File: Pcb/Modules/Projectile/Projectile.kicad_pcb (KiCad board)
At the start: 2 copper layers, 108.7 x 45.7 mm, 39 parts, among them J1 JACK_RJ45, Q1 Q_NMOS_GSD, Q2 Q_NMOS_GSD, U1 OPA320, U2 OPA320, X1 HOLE, X2 HOLE, X3 HOLE, X4 HOLE

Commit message: Add some missing text to silkscreen.  Move mount holes by 5 mils.
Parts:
- moved X1 0.13 mm to (112.5, 66.0)
- moved X4 0.13 mm to (112.5, 27.9)
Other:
- board text added: "Light1"
- board text added: "Light2"
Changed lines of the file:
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@@
     (area 25.683869 23.4618 137.997001 70.6182)
     (thickness 1.6)
-    (drawings 5)
+    (drawings 15)
     (tracks 220)
     (zones 0)
@@
     (zone_45_only yes)
     (trace_min 0.2)
-    (segment_width 0.2)
+    (segment_width 2.54)
     (edge_width 0.15)
     (via_size 0.6604)
@@
   )
   (module Mounting_Holes:MountingHole_2.5mm_Pad (layer F.Cu)
-    (at 112.395 66.04)
+    (at 112.522 66.04)
     (descr "Mounting Hole 2.5mm")
     (tags "mounting hole 2.5mm")
@@
   )
   (module Mounting_Holes:MountingHole_2.5mm_Pad (layer F.Cu)
-    (at 112.395 27.94)
+    (at 112.522 27.94)
     (descr "Mounting Hole 2.5mm")
     (tags "mounting hole 2.5mm")
@@
     )
   )
+  (gr_text Light2 (at 137.668 48.387) (layer F.SilkS)
+    (effects (font (size 1.5 1.5) (thickness 0.3)) (justify right))
+  )
+  (gr_text Light1 (at 29.337 48.387) (layer F.SilkS)
+    (effects (font (size 1.5 1.5) (thickness 0.3)) (justify left))
+  )
+  (gr_line (start 105.41 57.15) (end 104.14 57.15) (angle 90) (layer F.SilkS) (width 2.54))
+  (gr_line (start 105.41 60.96) (end 105.41 57.15) (angle 90) (layer F.SilkS) (width 2.54))
+  (gr_line (start 102.87 63.5) (end 105.41 60.96) (angle 90) (layer F.SilkS) (width 2.54))
+  (gr_line (start 102.87 55.88) (end 102.87 63.5) (angle 90) (layer F.SilkS) (width 2.54))
+  (gr_line (start 101.6 67.31) (end 109.22 59.69) (angle 90) (layer F.SilkS) (width 2.54))
+  (gr_line (start 101.6 52.07) (end 101.6 67.31) (angle 90) (layer F.SilkS) (width 2.54))
+  (gr_line (start 109.22 59.69) (end 101.6 52.07) (angle 90) (layer F.SilkS) (width 2.54))
+  (gr_line (start 55.88 59.69) (end 109.22 59.69) (angle 90) (layer F.SilkS) (width 2.54))
   (gr_line (start 137.922 69.85) (end 137.922 24.13) (angle 90) (layer Edge.Cuts) (width 0.15))
   (gr_line (start 29.21 24.13) (end 29.21 69.85) (angle 90) (layer Edge.Cuts) (width 0.15))

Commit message: Update module pcbs
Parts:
- D1, D2, D3, D4, D5, D6: moved to B.Cu
- J1: moved to F.Cu
- moved D1 2.54 mm to (32.8, 61.0), turned to 90 degrees
- moved D2 2.54 mm to (32.8, 54.4), turned to 90 degrees
- moved D4 2.54 mm to (134.4, 54.4), turned to 90 degrees
- moved D6 2.54 mm to (134.4, 61.0), turned to 90 degrees
- moved D3 2.54 mm to (32.8, 67.6), turned to 90 degrees
- moved D5 2.54 mm to (134.4, 67.6), turned to 90 degrees
- turned J1 to 270 degrees
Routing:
- net 3V3: track 270.9 -> 259.6 mm
- net Net-(D4-Pad1): track 21.0 -> 29.8 mm
- net Net-(D2-Pad1): track 21.9 -> 28.2 mm
- net Net-(J1-Pad3): track 101.4 -> 104.8 mm
- net Net-(J1-Pad2): track 60.7 -> 62.1 mm, vias 0 -> 1
- net Net-(C6-Pad2): track 9.62 -> 8.58 mm
- net Net-(J1-Pad4): track 114.4 -> 113.7 mm
- net Net-(C4-Pad2): track 8.79 -> 9.41 mm
- net Net-(D2-Pad2): track 4.35 -> 4.86 mm
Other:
- board text added: "Projectile Module 2018.3.31"
- board text removed: "Projectile Module 2017.12.23"

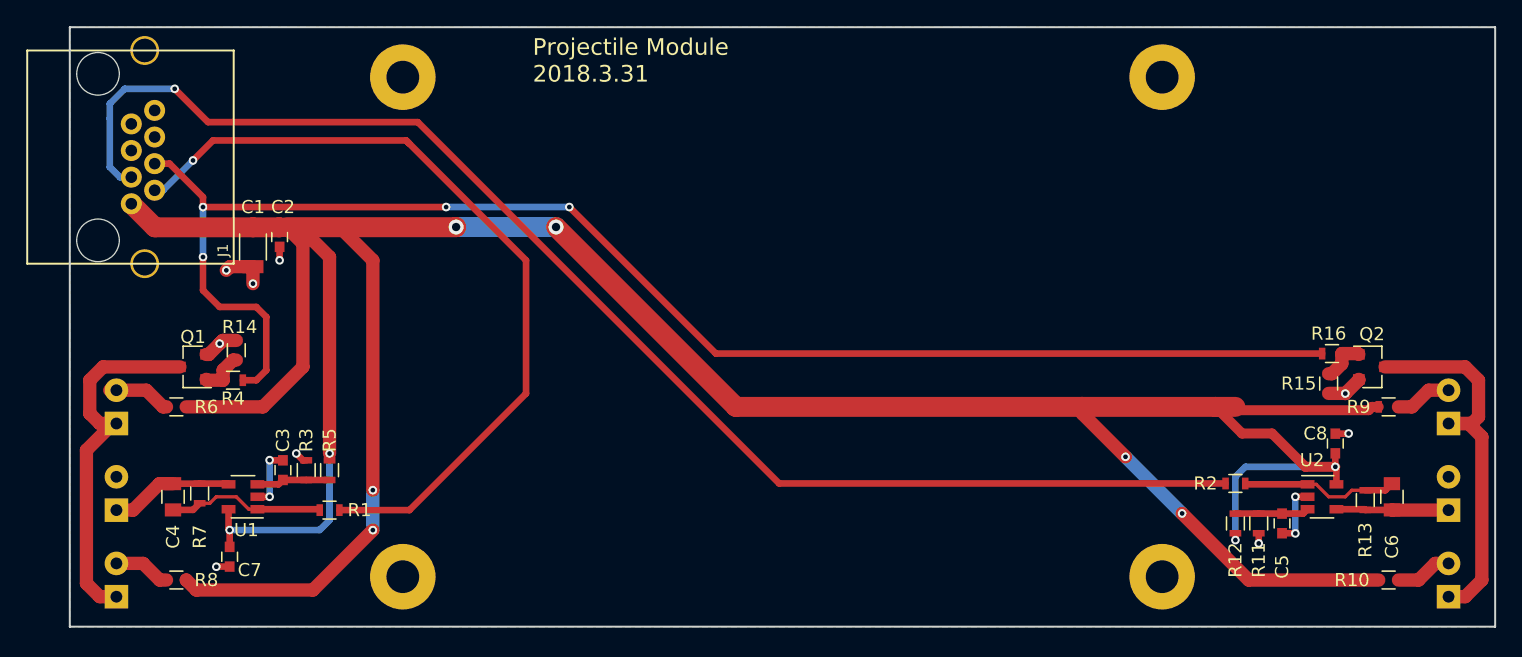
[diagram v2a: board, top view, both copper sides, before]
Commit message: Update module pcbs to fix minor issues and round corners
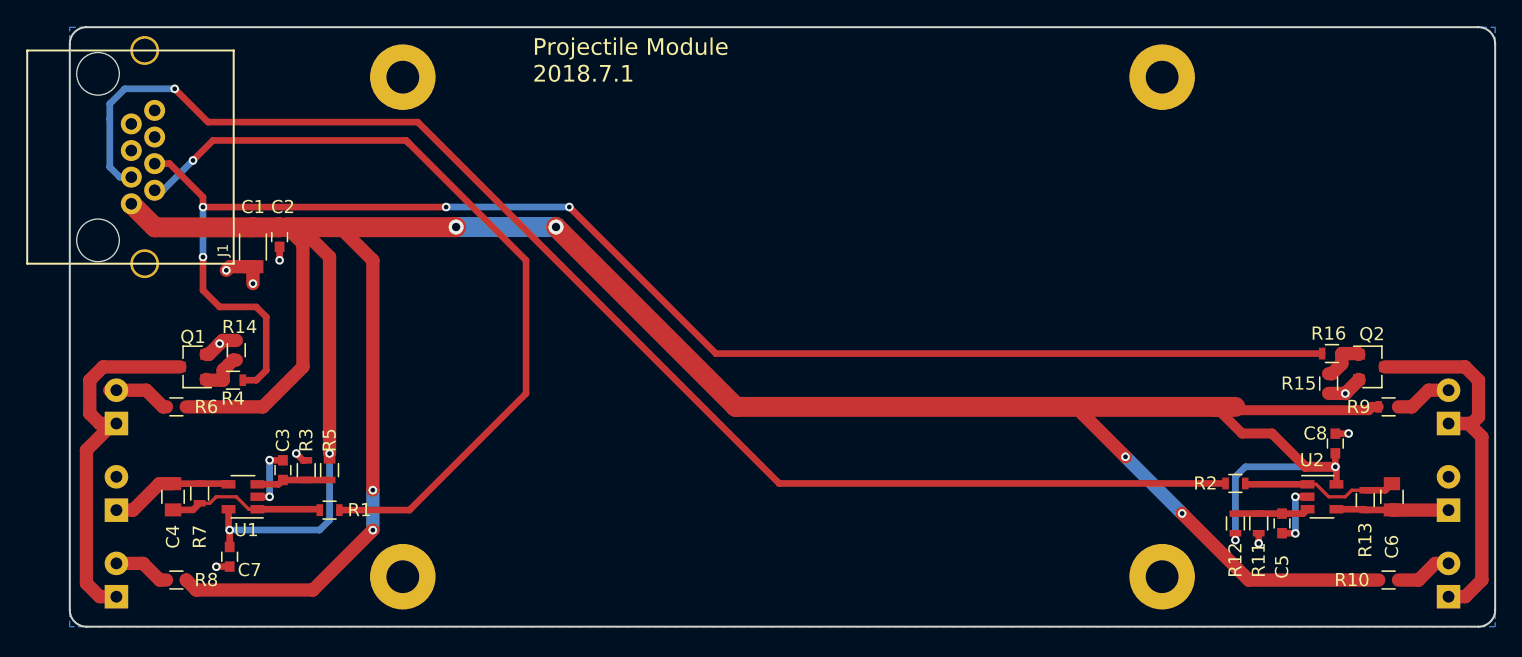
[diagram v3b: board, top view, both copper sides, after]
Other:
- outline, holes or cut-outs redrawn
- board text added: "Projectile Module 2018.7.1"
- board text removed: "Projectile Module 2018.3.31"
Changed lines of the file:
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@@
     (area 25.683869 23.4618 137.997001 70.6182)
     (thickness 1.6)
-    (drawings 15)
+    (drawings 19)
     (tracks 229)
     (zones 0)
@@
     )
   )
+  (gr_line (start 29.21 68.58) (end 29.21 25.4) (angle 90) (layer Edge.Cuts) (width 0.15))
+  (gr_line (start 136.652 69.85) (end 30.48 69.85) (angle 90) (layer Edge.Cuts) (width 0.15))
+  (gr_line (start 137.922 25.4) (end 137.922 68.58) (angle 90) (layer Edge.Cuts) (width 0.15))
+  (gr_line (start 30.48 24.13) (end 136.652 24.13) (angle 90) (layer Edge.Cuts) (width 0.15))
+  (gr_arc (start 30.48 68.58) (end 30.48 69.85) (angle 90) (layer Edge.Cuts) (width 0.15))
+  (gr_arc (start 30.48 25.4) (end 29.21 25.4) (angle 90) (layer Edge.Cuts) (width 0.15))
+  (gr_arc (start 136.652 25.4) (end 136.652 24.13) (angle 90) (layer Edge.Cuts) (width 0.15))
+  (gr_arc (start 136.652 68.58) (end 137.922 68.58) (angle 90) (layer Edge.Cuts) (width 0.15))
   (gr_line (start 55.88 59.69) (end 109.22 59.69) (angle 90) (layer B.SilkS) (width 2.54))
   (gr_text Light2 (at 130.81 48.514) (layer B.SilkS)
@@
   (gr_line (start 101.6 52.07) (end 101.6 67.31) (angle 90) (layer B.SilkS) (width 2.54))
   (gr_line (start 109.22 59.69) (end 101.6 52.07) (angle 90) (layer B.SilkS) (width 2.54))
-  (gr_line (start 137.922 69.85) (end 137.922 24.13) (angle 90) (layer Edge.Cuts) (width 0.15))
-  (gr_line (start 29.21 24.13) (end 29.21 69.85) (angle 90) (layer Edge.Cuts) (width 0.15))
-  (gr_line (start 137.922 24.13) (end 29.21 24.13) (angle 90) (layer Edge.Cuts) (width 0.15))
-  (gr_line (start 29.21 69.85) (end 137.922 69.85) (angle 90) (layer Edge.Cuts) (width 0.15))
-  (gr_text "Projectile Module\n2018.3.31" (at 64.516 26.67) (layer F.SilkS)
+  (gr_text "Projectile Module\n2018.7.1" (at 64.516 26.67) (layer F.SilkS)
     (effects (font (size 1.27 1.27) (thickness 0.254)) (justify left))
   )
